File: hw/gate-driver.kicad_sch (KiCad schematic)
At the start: 16 parts

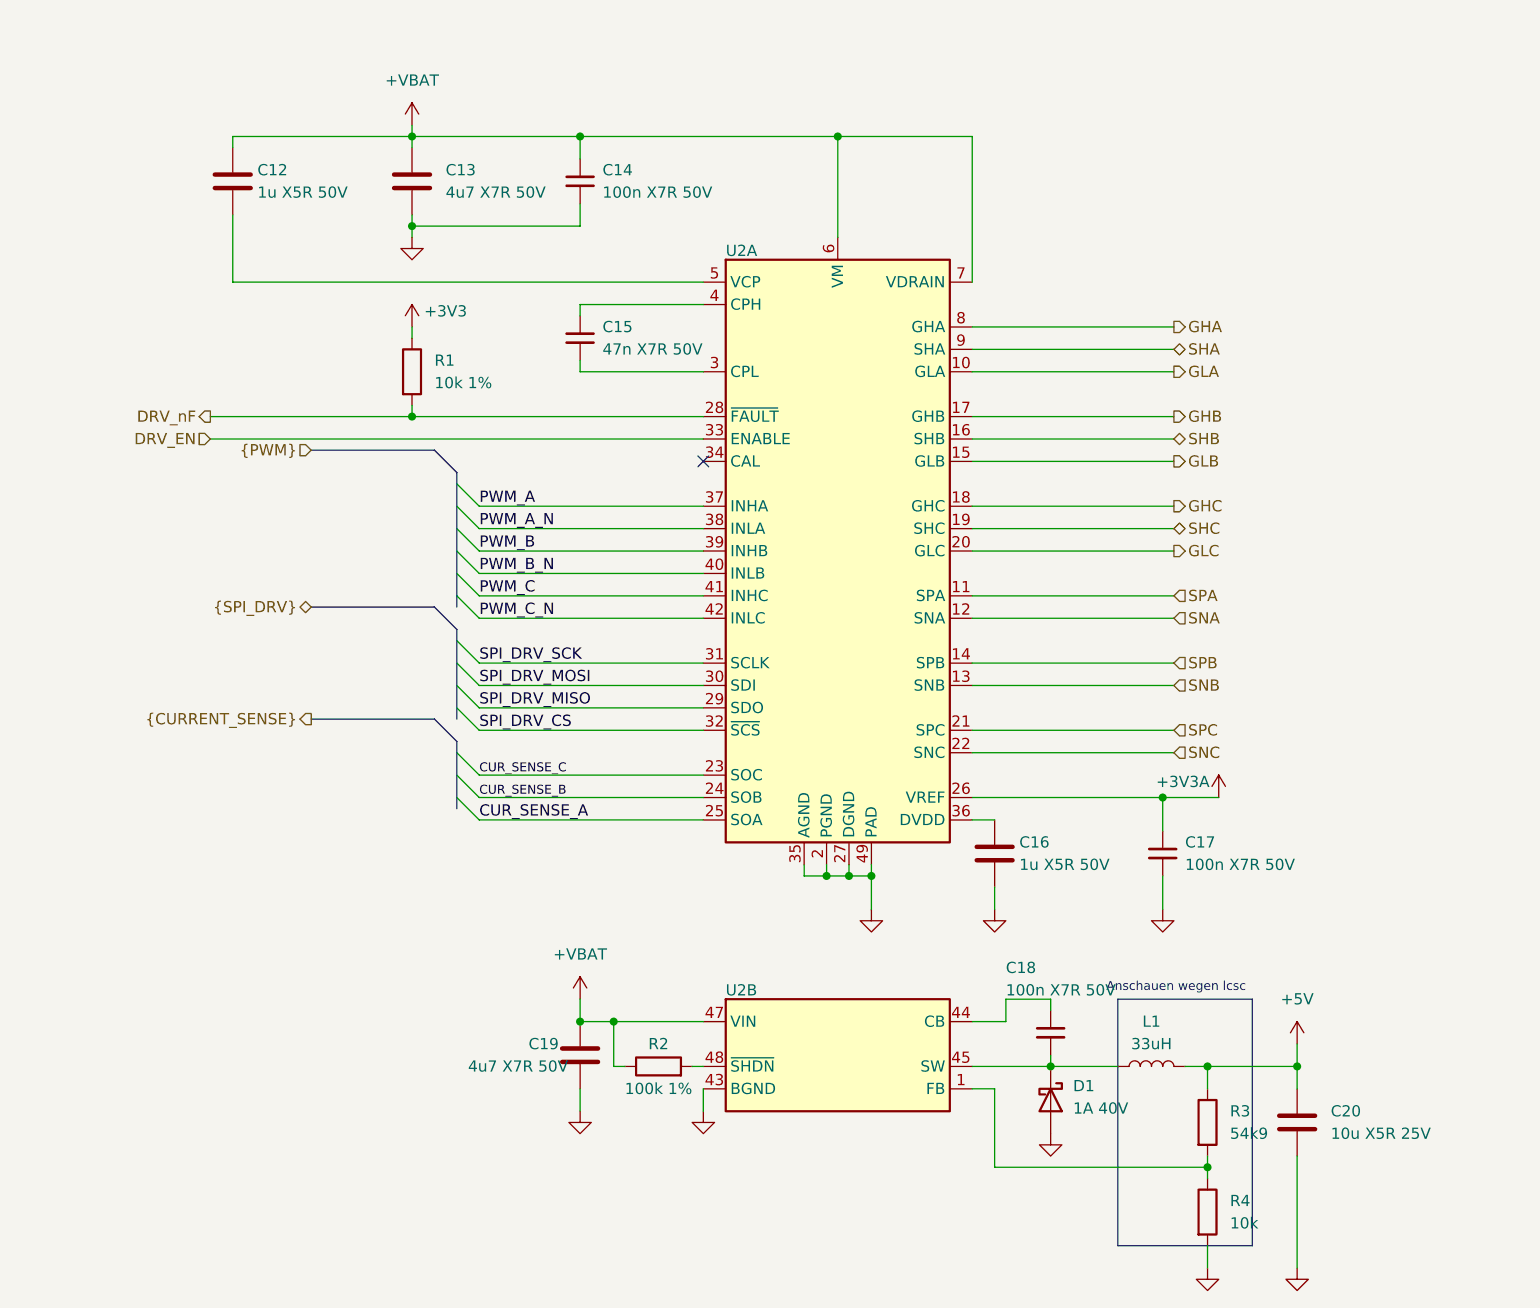
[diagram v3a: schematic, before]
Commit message: cleaned up *.kicad_sch
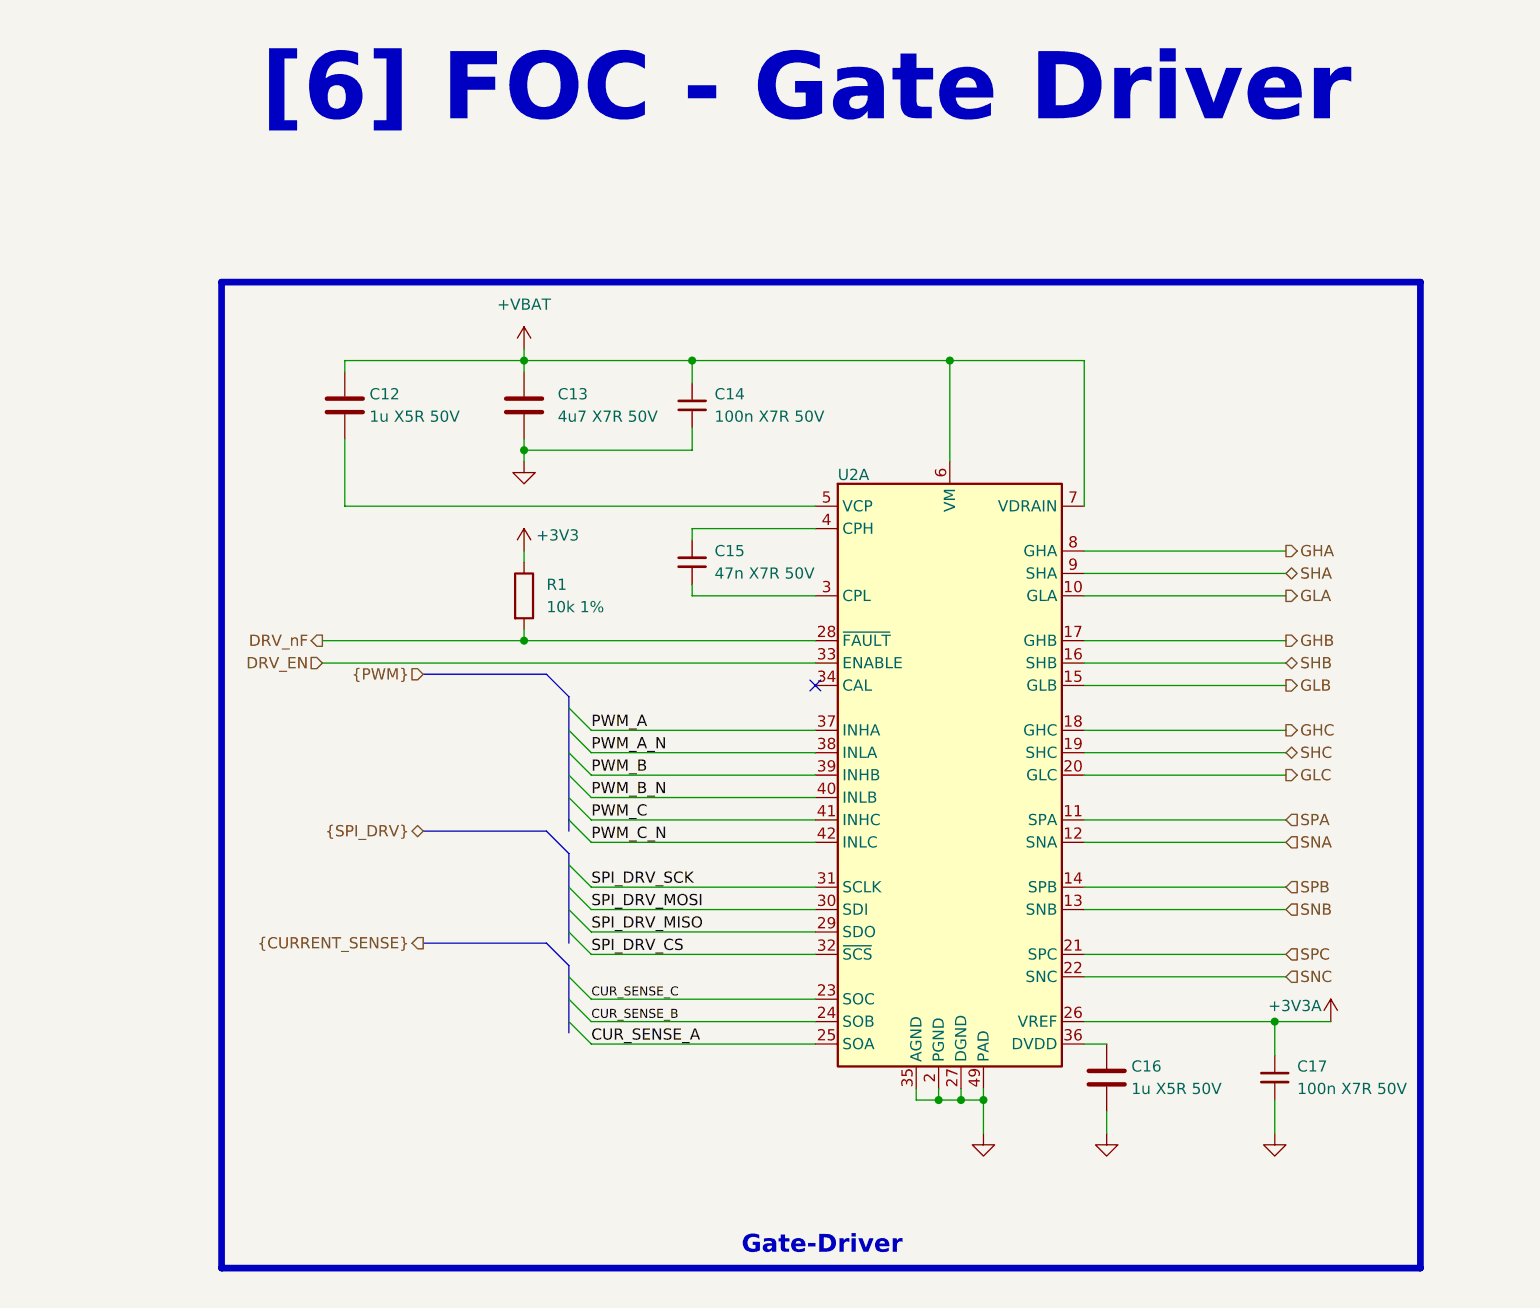
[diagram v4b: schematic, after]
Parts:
- removed C18: 100n X7R 50V, Capacitor_SMD:C_0603_1608Metric, symbol Device:C_Small
- removed C19: 4u7 X7R 50V, Capacitor_SMD:C_1206_3216Metric, symbol Device:C
- removed C20: 10u X5R 25V, Capacitor_SMD:C_0805_2012Metric, symbol Device:C
- removed D1: 1A 40V, Diode_SMD:D_SOD-123, symbol Device:D_Schottky
- removed L1: 33uH, Inductor_SMD:L_APV_ANR6020, symbol Device:L
- removed R2: 100k 1%, Resistor_SMD:R_0603_1608Metric, symbol Device:R
- removed R3: 54k9, symbol Device:R
- removed R4: 10k, symbol Device:R
- removed unit 2 of U2
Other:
- note added: "Gate-Driver"
- note added: "[6] FOC - Gate Driver"
- note removed: "Anschauen wegen lcsc"
- title: (none) -> FOC - Gate Driver
- moved on the sheet: C12, C13, C14, C15, C16, C17, R1, U2A
